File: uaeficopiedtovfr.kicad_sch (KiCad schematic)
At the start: 38 parts, among them J1 USB_B_Mini, J1 USB_C_Receptacle_USB2.0, J17 Conn_01x06, J4 1-776087-1, J7 MUSBD111M0, M1 Module-power_12and5V-0.2, M3 Module-knock-0.2, M3 Module-vr-discrete-0.4, M4 Module-vr-max9924-0.1, M5 Module-wbo-0.5, M6 Module:mega-mcu100/0.2, M7 Module-wbo-0.5, P1 Pad, P2 Pad, P3 Pad, P4 Pad, U4 JDY-33

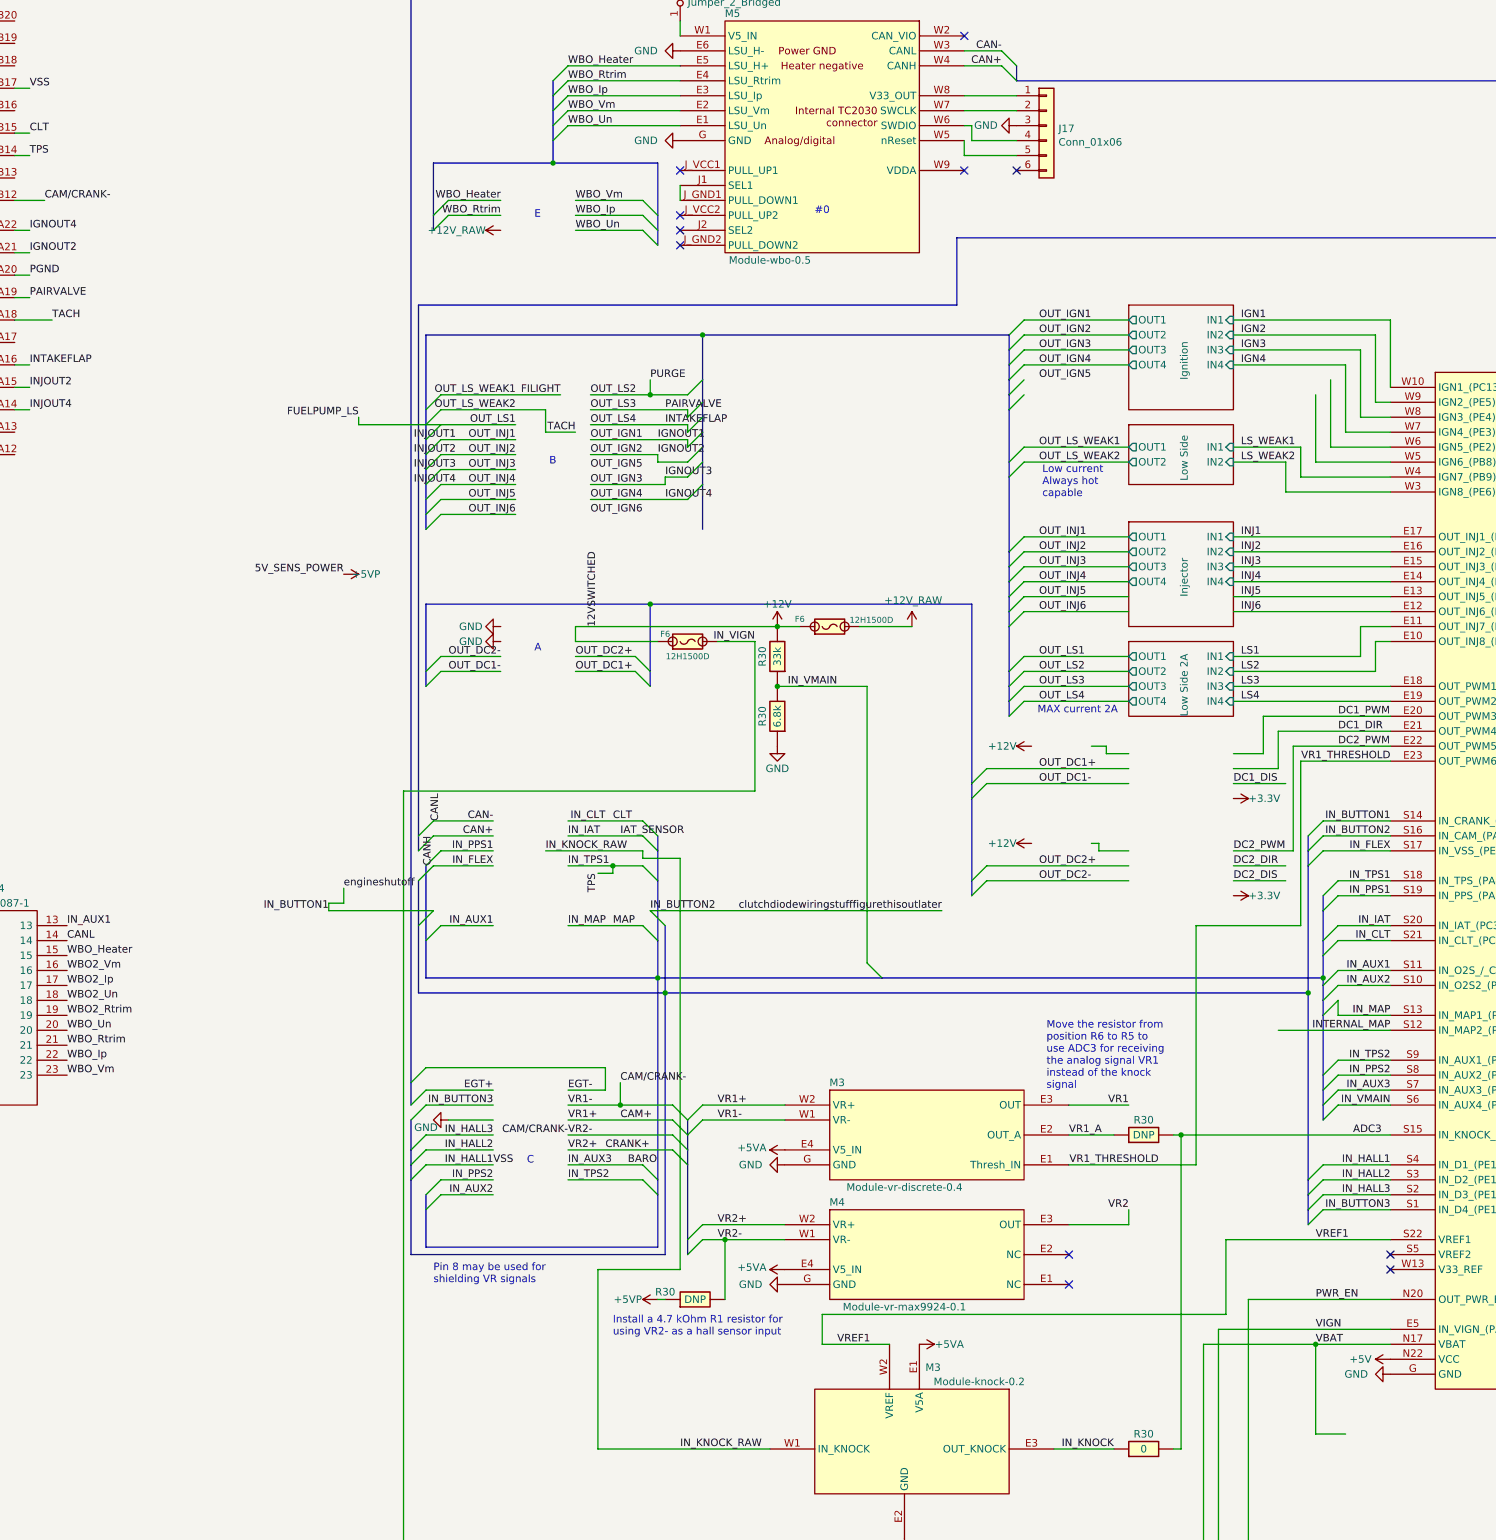
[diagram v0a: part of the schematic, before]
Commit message: Added VR- offset resistors and pads for unused analog/hall inputs
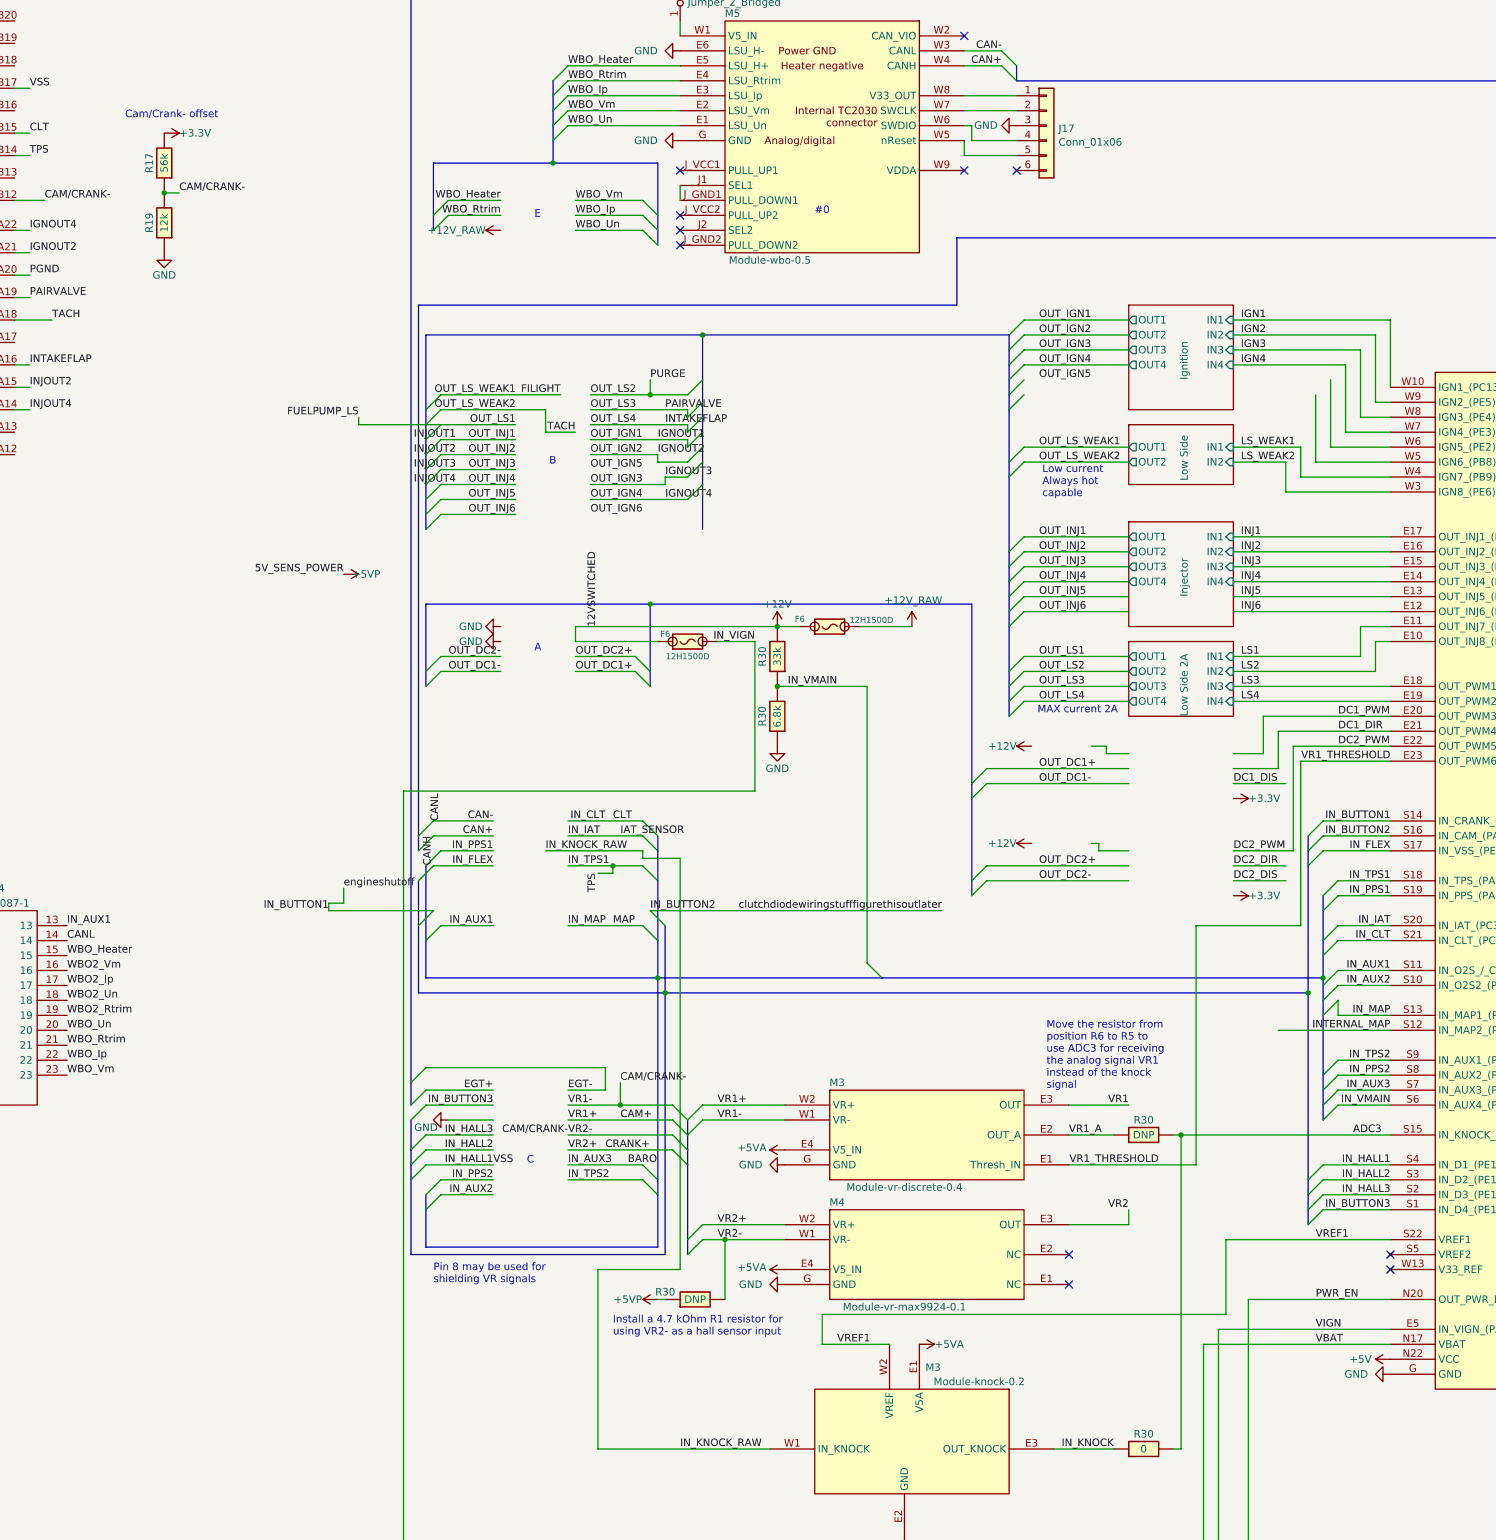
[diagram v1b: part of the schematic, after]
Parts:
- added R17: 56k, hellen-one-common:R0603, symbol hellen-one-common:Res
- added R19: 12k, hellen-one-common:R0603, symbol hellen-one-common:Res
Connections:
- net +3.3V: now also R17.2
- net CAM/CRANK-: now also R17.1, R19.2
- net GND: now also R19.1
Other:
- note added: "Cam/Crank- offset"
